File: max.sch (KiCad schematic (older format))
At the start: 48 parts, among them P4 ttyMAX3, P5 ttyMAX2, P6 ttyMAX1, P7 ttyMAX0, SW2 DIP_SW4, U8 SG-210STF_16MHz, U9 MAX14830

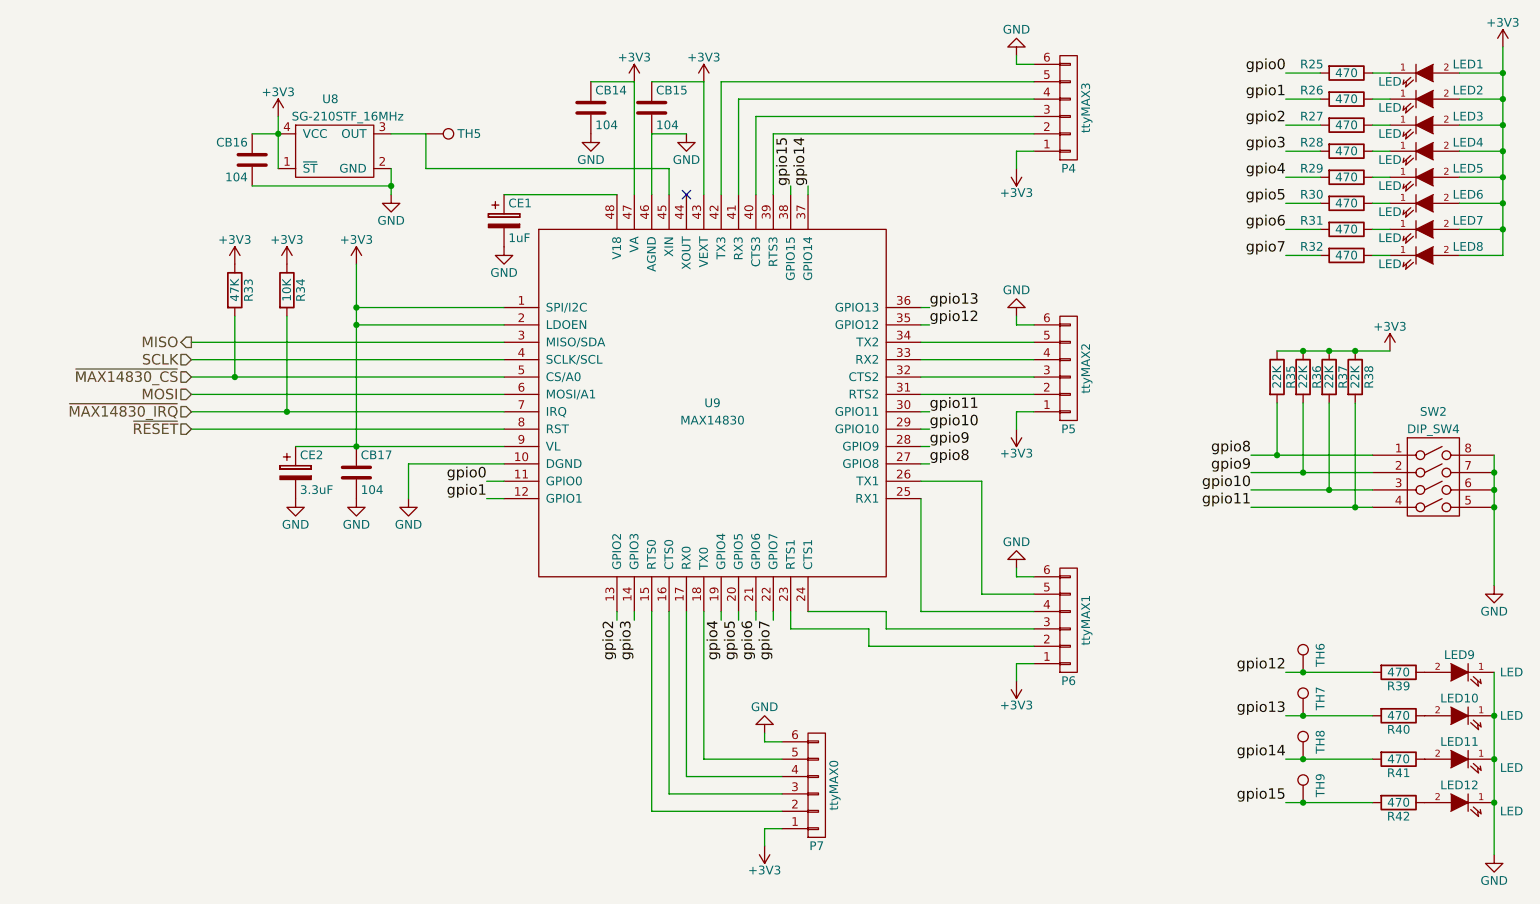
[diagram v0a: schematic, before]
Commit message: Deleted unnecessary files and splitting schmatics.
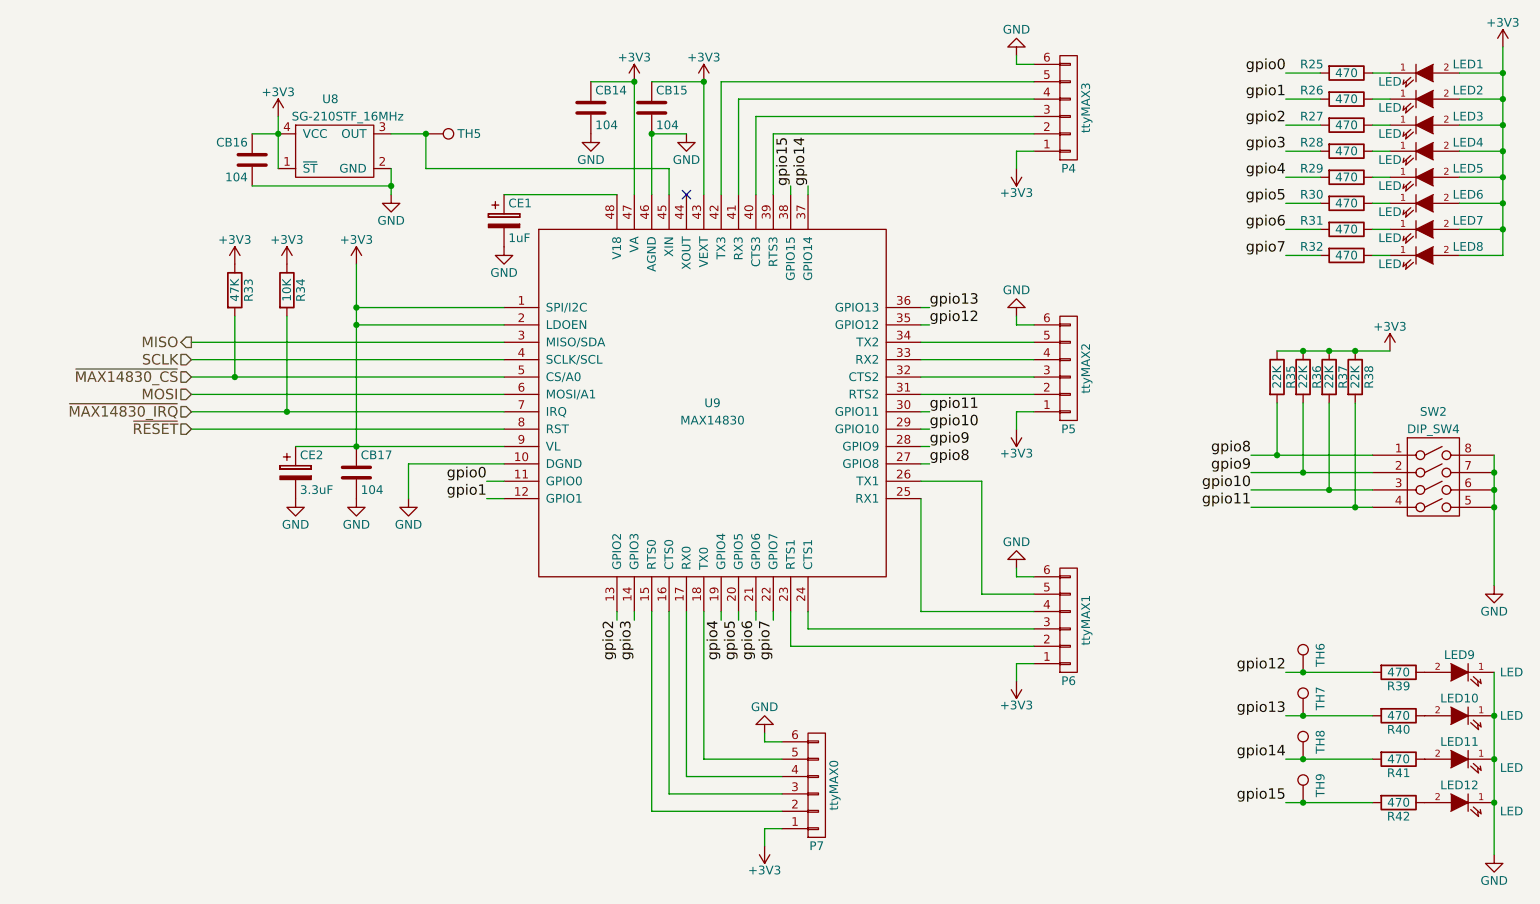
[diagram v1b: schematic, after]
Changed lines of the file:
@@
 $Descr A4 11693 8268
 encoding utf-8
-Sheet 3 6
-Title ""
+Sheet 3 8
+Title "DCoJA Yatagarasu Mezzanine"
 Date ""
 Rev ""
-Comp ""
-Comment1 ""
-Comment2 ""
-Comment3 ""
-Comment4 ""
+Comp "DroneWorks Inc."
+Comment1 "Copyright (c) 2016 DroneWorks Inc."
+Comment2 "All rights reserved."
+Comment3 "Creative Commons  (CC BY-SA 4.0)"
+Comment4 "Designed by: Michihiro Imaoka (@imaoca)"
+Comment5 "Serial ports"
 $EndDescr
 $Comp
@@
 $EndComp
 $Comp
-L GND #PWR058
+L GND #PWR046
 U 1 1 56F7B77C
 P 3200 3950
-F 0 "#PWR058" H 3200 3700 50  0001 C CNN
+F 0 "#PWR046" H 3200 3700 50  0001 C CNN
 F 1 "GND" H 3200 3800 50  0000 C CNN
 F 2 "" H 3200 3950 60  0000 C CNN
@@
 $EndComp
 $Comp
-L GND #PWR059
+L GND #PWR047
 U 1 1 56F7B796
 P 6700 1400
-F 0 "#PWR059" H 6700 1150 50  0001 C CNN
+F 0 "#PWR047" H 6700 1150 50  0001 C CNN
 F 1 "GND" H 6700 1250 50  0000 C CNN
 F 2 "" H 6700 1400 60  0000 C CNN
@@
 $EndComp
 $Comp
-L GND #PWR060
+L GND #PWR048
 U 1 1 56F7B7A9
 P 6700 2900
-F 0 "#PWR060" H 6700 2650 50  0001 C CNN
+F 0 "#PWR048" H 6700 2650 50  0001 C CNN
 F 1 "GND" H 6700 2750 50  0000 C CNN
 F 2 "" H 6700 2900 60  0000 C CNN
@@
 $EndComp
 $Comp
-L GND #PWR061
+L GND #PWR049
 U 1 1 56F7B7BC
 P 6700 4350
-F 0 "#PWR061" H 6700 4100 50  0001 C CNN
+F 0 "#PWR049" H 6700 4100 50  0001 C CNN
 F 1 "GND" H 6700 4200 50  0000 C CNN
 F 2 "" H 6700 4350 60  0000 C CNN
@@
 $EndComp
 $Comp
-L GND #PWR062
+L GND #PWR050
 U 1 1 56F7B7CF
 P 5250 5300
-F 0 "#PWR062" H 5250 5050 50  0001 C CNN
+F 0 "#PWR050" H 5250 5050 50  0001 C CNN
 F 1 "GND" H 5250 5150 50  0000 C CNN
 F 2 "" H 5250 5300 60  0000 C CNN
@@
 $EndComp
 $Comp
-L GND #PWR063
+L GND #PWR051
 U 1 1 56FF154F
 P 9450 6000
-F 0 "#PWR063" H 9450 5750 50  0001 C CNN
+F 0 "#PWR051" H 9450 5750 50  0001 C CNN
 F 1 "GND" H 9450 5850 50  0000 C CNN
 F 2 "" H 9450 6000 60  0000 C CNN
@@
 $EndComp
 $Comp
-L GND #PWR064
+L GND #PWR052
 U 1 1 56FF190C
 P 9450 4450
-F 0 "#PWR064" H 9450 4200 50  0001 C CNN
+F 0 "#PWR052" H 9450 4200 50  0001 C CNN
 F 1 "GND" H 9450 4300 50  0000 C CNN
 F 2 "" H 9450 4450 60  0000 C CNN
@@
 NoConn ~ 4800 2200
 $Comp
-L GND #PWR065
+L GND #PWR053
 U 1 1 56FEE288
 P 3100 2200
-F 0 "#PWR065" H 3100 1950 50  0001 C CNN
+F 0 "#PWR053" H 3100 1950 50  0001 C CNN
 F 1 "GND" H 3100 2050 50  0000 C CNN
 F 2 "" H 3100 2200 50  0000 C CNN
@@
 $EndComp
 $Comp
-L GND #PWR066
+L GND #PWR054
 U 1 1 5705B8B8
 P 3750 2500
-F 0 "#PWR066" H 3750 2250 50  0001 C CNN
+F 0 "#PWR054" H 3750 2250 50  0001 C CNN
 F 1 "GND" H 3750 2350 50  0000 C CNN
 F 2 "" H 3750 2500 60  0000 C CNN
@@
 $EndComp
 $Comp
-L GND #PWR067
+L GND #PWR055
 U 1 1 57061BCC
 P 2900 3950
-F 0 "#PWR067" H 2900 3700 50  0001 C CNN
+F 0 "#PWR055" H 2900 3700 50  0001 C CNN
 F 1 "GND" H 2900 3800 50  0000 C CNN
 F 2 "" H 2900 3950 60  0000 C CNN
@@
 $EndComp
 $Comp
-L GND #PWR068
+L GND #PWR056
 U 1 1 57063190
 P 4250 1850
-F 0 "#PWR068" H 4250 1600 50  0001 C CNN
+F 0 "#PWR056" H 4250 1600 50  0001 C CNN
 F 1 "GND" H 4250 1700 50  0000 C CNN
 F 2 "" H 4250 1850 60  0000 C CNN
@@
 $EndComp
 $Comp
-L GND #PWR069
+L GND #PWR057
 U 1 1 5706380D
 P 4800 1850
-F 0 "#PWR069" H 4800 1600 50  0001 C CNN
+F 0 "#PWR057" H 4800 1600 50  0001 C CNN
 F 1 "GND" H 4800 1700 50  0000 C CNN
 F 2 "" H 4800 1850 60  0000 C CNN
@@
 	5250 5350 5350 5350
 Wire Wire Line
-	5400 4600 5400 4700
+	5400 4600 5400 4800
 Wire Wire Line
 	5000 2200 5000 1550
@@
 	2550 3650 3750 3650
 $Comp
-L +3V3 #PWR070
+L +3V3 #PWR058
 U 1 1 57070627
 P 2450 1750
-F 0 "#PWR070" H 2450 1600 50  0001 C CNN
+F 0 "#PWR058" H 2450 1600 50  0001 C CNN
 F 1 "+3V3" H 2450 1890 50  0000 C CNN
 F 2 "" H 2450 1750 50  0000 C CNN
@@
 $EndComp
 $Comp
-L +3V3 #PWR071
+L +3V3 #PWR059
 U 1 1 5707075A
 P 2200 2600
-F 0 "#PWR071" H 2200 2450 50  0001 C CNN
+F 0 "#PWR059" H 2200 2450 50  0001 C CNN
 F 1 "+3V3" H 2200 2740 50  0000 C CNN
 F 2 "" H 2200 2600 50  0000 C CNN
@@
 $EndComp
 $Comp
-L +3V3 #PWR072
+L +3V3 #PWR060
 U 1 1 570707F5
 P 2500 2600
-F 0 "#PWR072" H 2500 2450 50  0001 C CNN
+F 0 "#PWR060" H 2500 2450 50  0001 C CNN
 F 1 "+3V3" H 2500 2740 50  0000 C CNN
 F 2 "" H 2500 2600 50  0000 C CNN
@@
 $EndComp
 $Comp
-L +3V3 #PWR073
+L +3V3 #PWR061
 U 1 1 5707088E
 P 2900 2600
-F 0 "#PWR073" H 2900 2450 50  0001 C CNN
+F 0 "#PWR061" H 2900 2450 50  0001 C CNN
 F 1 "+3V3" H 2900 2740 50  0000 C CNN
 F 2 "" H 2900 2600 50  0000 C CNN
@@
 $EndComp
 $Comp
-L +3V3 #PWR074
+L +3V3 #PWR062
 U 1 1 57070925
 P 4500 1550
-F 0 "#PWR074" H 4500 1400 50  0001 C CNN
+F 0 "#PWR062" H 4500 1400 50  0001 C CNN
 F 1 "+3V3" H 4500 1690 50  0000 C CNN
 F 2 "" H 4500 1550 50  0000 C CNN
@@
 $EndComp
 $Comp
-L +3V3 #PWR075
+L +3V3 #PWR063
 U 1 1 570709BC
 P 4900 1550
-F 0 "#PWR075" H 4900 1400 50  0001 C CNN
+F 0 "#PWR063" H 4900 1400 50  0001 C CNN
 F 1 "+3V3" H 4900 1690 50  0000 C CNN
 F 2 "" H 4900 1550 50  0000 C CNN
@@
 $EndComp
 $Comp
-L +3V3 #PWR076
+L +3V3 #PWR064
 U 1 1 57070A53
 P 6700 2050
-F 0 "#PWR076" H 6700 1900 50  0001 C CNN
+F 0 "#PWR064" H 6700 1900 50  0001 C CNN
 F 1 "+3V3" H 6700 2190 50  0000 C CNN
 F 2 "" H 6700 2050 50  0000 C CNN
@@
 $EndComp
 $Comp
-L +3V3 #PWR077
+L +3V3 #PWR065
 U 1 1 57070AEA
 P 6700 3550
-F 0 "#PWR077" H 6700 3400 50  0001 C CNN
+F 0 "#PWR065" H 6700 3400 50  0001 C CNN
 F 1 "+3V3" H 6700 3690 50  0000 C CNN
 F 2 "" H 6700 3550 50  0000 C CNN
@@
 $EndComp
 $Comp
-L +3V3 #PWR078
+L +3V3 #PWR066
 U 1 1 570715D1
 P 6700 5000
-F 0 "#PWR078" H 6700 4850 50  0001 C CNN
+F 0 "#PWR066" H 6700 4850 50  0001 C CNN
 F 1 "+3V3" H 6700 5140 50  0000 C CNN
 F 2 "" H 6700 5000 50  0000 C CNN
@@
 $EndComp
 $Comp
-L +3V3 #PWR079
+L +3V3 #PWR067
 U 1 1 57072088
 P 5250 5950
-F 0 "#PWR079" H 5250 5800 50  0001 C CNN
+F 0 "#PWR067" H 5250 5800 50  0001 C CNN
 F 1 "+3V3" H 5250 6090 50  0000 C CNN
 F 2 "" H 5250 5950 50  0000 C CNN
@@
 $EndComp
 $Comp
-L +3V3 #PWR080
+L +3V3 #PWR068
 U 1 1 570A6A75
 P 9500 1350
-F 0 "#PWR080" H 9500 1200 50  0001 C CNN
+F 0 "#PWR068" H 9500 1200 50  0001 C CNN
 F 1 "+3V3" H 9500 1490 50  0000 C CNN
 F 2 "" H 9500 1350 50  0000 C CNN
@@
 $EndComp
 $Comp
-L +3V3 #PWR081
+L +3V3 #PWR069
 U 1 1 570A6AE9
 P 8850 3100
-F 0 "#PWR081" H 8850 2950 50  0001 C CNN
+F 0 "#PWR069" H 8850 2950 50  0001 C CNN
 F 1 "+3V3" H 8850 3240 50  0000 C CNN
 F 2 "" H 8850 3100 50  0000 C CNN
@@
 $EndComp
 $Comp
-L GND #PWR082
+L GND #PWR070
 U 1 1 570B00C6
 P 2550 3950
-F 0 "#PWR082" H 2550 3700 50  0001 C CNN
+F 0 "#PWR070" H 2550 3700 50  0001 C CNN
 F 1 "GND" H 2550 3800 50  0000 C CNN
 F 2 "" H 2550 3950 60  0000 C CNN
@@
 	6150 4600 6800 4600
 Wire Wire Line
-	5500 4600 5950 4600
-Wire Wire Line
-	5950 4600 5950 4700
-Wire Wire Line
-	5950 4700 6800 4700
-Wire Wire Line
-	5400 4700 5850 4700
-Wire Wire Line
-	5850 4700 5850 4800
-Wire Wire Line
-	5850 4800 6800 4800
+	5500 4700 6800 4700
+Wire Wire Line
+	5400 4800 6800 4800
 Wire Wire Line
 	4900 4600 4900 5450
@@
 Wire Wire Line
 	4600 5750 5350 5750
+Connection ~ 3300 1850
+Connection ~ 4500 1550
+Connection ~ 4900 1550
+Wire Wire Line
+	5500 4700 5500 4600
+Connection ~ 4600 1850
 $EndSCHEMATC
